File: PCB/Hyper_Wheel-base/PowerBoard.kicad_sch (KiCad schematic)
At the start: 19 parts, among them J2 LIPO, U1 CSD85301Q2, U10 TPS22916CNYFPR, U4 TPS22916CNYFPR, U5 TPS78233DDCR, U6 BQ29700DSER, U7 BQ24074RGTR, U9 CSD85301Q2

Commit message: Base Push
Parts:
- added Rdiv1: 150k, Resistor_SMD:R_0603_1608Metric, symbol Device:R
- added Rdiv2: 300k, Resistor_SMD:R_0603_1608Metric, symbol Device:R
- added U12: TPS22916CNYFPR, Hyper_Wheel:TPS22916-YFP0004ABAB, symbol TPS22916CNYFPR:TPS22916CNYFPR
- CP4: renamed from C4; footprint Capacitor_SMD:C_0201_0603Metric_Pad0.64x0.40mm_HandSolder -> (none)
- J2: footprint (none) -> Connector_JST:JST_EH_B2B-EH-A_1x02_P2.50mm_Vertical
- U1, U9: footprint DQK0006B -> Hyper_Wheel:CDS85301-DQK0006B
- U10, U4: footprint YFP0004ABAB -> Hyper_Wheel:TPS22916-YFP0004ABAB
- U6: footprint DSE0006A -> Hyper_Wheel:BQ29700-DSE0006A
- U7: footprint BQ24074RGTR:QFN50P300X300X100-17N -> Hyper_Wheel:BQ24074-QFN50P300X300X100-17N
- renumbered C1 to CP1, C2 to CP2, C3 to CP3, D1 to DP1, R1 to RP1, R2 to RP2, R3 to RP3, R4 to RP4, R5 to RP5, R6 to RP6
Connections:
- net 3.3V_Regulated: now also U12.A2 (VIN); no longer CP4.1, U5.5 (OUT)
- net GND: now also Rdiv1.1, Rdiv2.2, U12.B1 (GND)
- net ChargerOut renamed ChargerOUT
- net LoadSwitch1EN renamed Load1_Ctrl
- net LoadSwitch1_Vout renamed Load1_Vout
- net LoadSwitch2EN renamed Load2_Ctrl
- net LoadSwitch2_Vout renamed Load2_Vout
- net USB+ renamed Charger+
- new net: CP4.1, U5.5 (OUT)
- new net Cell-Mon: Rdiv1.2, Rdiv2.1
- new net Load3_Ctrl: U12.B2 (ON)
- new net Load3_Vout: U12.A1 (VOUT)
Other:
- moved on the sheet: CP2, CP3, DP1, RP3, RP4, RP5, RP6, U7

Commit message: Main board nearing RevA completion
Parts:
- removed CP4: 1u, symbol Device:C
- removed U12: TPS22916CNYFPR, Hyper_Wheel:TPS22916-YFP0004ABAB, symbol TPS22916CNYFPR:TPS22916CNYFPR
- removed U5: TPS78233DDCR, DDC5_TEX, symbol TPS78233DDCR:TPS78233DDCR
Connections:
- net GND: no longer CP3.1, J2.1 (Pin_1), RP2.2, Rdiv1.1, U7.2 (BAT_2)
- net at U1.6 (D1), U9.6 (D1): now also U1.7 (D1), U9.7 (D1)
- new net Cell+: CP3.1, J2.1 (Pin_1), RP2.2, Rdiv1.1, U7.2 (BAT_2)

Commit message: Added test pads,
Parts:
- added P17, P18, P19, P20: TestPad, TestPoint:TestPoint_Pad_D2.0mm, symbol Connector:Conn_01x01_Pin
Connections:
- net Cell+: now also P17.1 (Pin_1)
- net Cell-: now also P18.1 (Pin_1)
- net ChargerOUT: now also P19.1 (Pin_1)
- net Prot-: now also P20.1 (Pin_1)

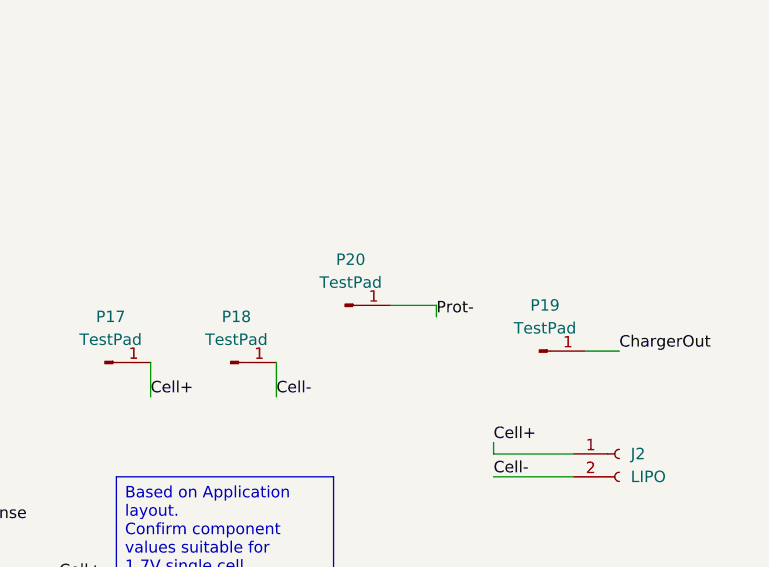
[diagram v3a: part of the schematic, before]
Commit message: XIAO based test board complete
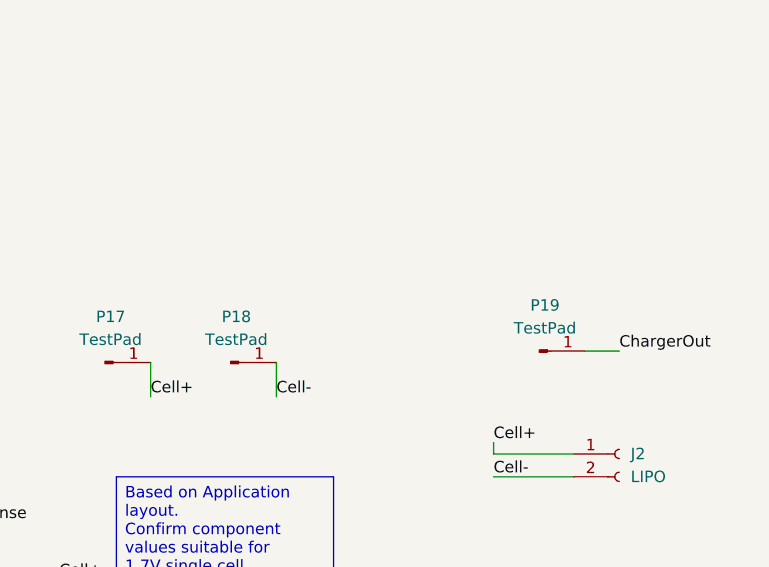
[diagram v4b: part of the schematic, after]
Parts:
- removed P20: TestPad, TestPoint:TestPoint_Pad_D2.0mm, symbol Connector:Conn_01x01_Pin
- CP1, CP2, CP3, DP1, RP1, RP2, RP3, RP4, RP5, RP6, Rdiv1, Rdiv2: KiLib_Generator (none) -> SMD_2terminal_chip_molded
- J2: KiLib_Generator (none) -> connector/JST
- P17, P18, P19: footprint TestPoint:TestPoint_Pad_D2.0mm -> TestPoint:TestPoint_Pad_D1.0mm; now left out of the parts list
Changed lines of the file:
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@@
 	(wire
 		(pts
-			(xy 245.11 71.12) (xy 245.11 72.39)
-		)
-		(stroke
-			(width 0)
-			(type default)
-		)
-	)
-	(wire
-		(pts
 			(xy 101.6 72.39) (xy 109.22 72.39)
 		)
@@
 	(wire
 		(pts
-			(xy 240.03 71.12) (xy 245.11 71.12)
-		)
-		(stroke
-			(width 0)
-			(type default)
-		)
-	)
-	(wire
-		(pts
 			(xy 193.04 137.16) (xy 193.04 162.56)
 		)
@@
 	)
 	(label "Prot-"
-		(at 245.11 72.39 0)
-		(effects
-			(font
-				(size 1.27 1.27)
-			)
-			(justify left bottom)
-		)
-	)
-	(label "Prot-"
 		(at 270.51 110.49 0)
 		(effects
@@
 			)
 		)
+		(property "KiLib_Generator" "SMD_2terminal_chip_molded"
+			(at 123.19 148.59 0)
+			(hide yes)
+			(show_name no)
+			(do_not_autoplace no)
+			(effects
+				(font
+					(size 1.27 1.27)
+				)
+			)
+		)
 		(pin "2"
 		)
@@
 			)
 		)
+		(property "KiLib_Generator" "SMD_2terminal_chip_molded"
+			(at 104.14 182.88 0)
+			(hide yes)
+			(show_name no)
+			(do_not_autoplace no)
+			(effects
+				(font
+					(size 1.27 1.27)
+				)
+			)
+		)
 		(pin "1"
 		)
@@
 		(body_style 1)
 		(exclude_from_sim no)
-		(in_bom yes)
+		(in_bom no)
 		(on_board yes)
 		(in_pos_files yes)
@@
 			)
 		)
-		(property "Footprint" "TestPoint:TestPoint_Pad_D2.0mm"
+		(property "Footprint" "TestPoint:TestPoint_Pad_D1.0mm"
 			(at 222.25 77.47 0)
 			(hide yes)
@@
 			)
 		)
-		(property "Description" "Generic connector, single row, 01x01, script generated"
+		(property "Description" ""
 			(at 222.25 77.47 0)
 			(hide yes)
@@
 	(symbol
 		(lib_id "Connector:Conn_01x01_Pin")
-		(at 234.95 71.12 0)
-		(unit 1)
-		(body_style 1)
-		(exclude_from_sim no)
-		(in_bom yes)
-		(on_board yes)
-		(in_pos_files yes)
-		(dnp no)
-		(fields_autoplaced yes)
-		(property "Reference" "P20"
-			(at 235.585 66.04 0)
-			(show_name no)
-			(do_not_autoplace no)
-			(effects
-				(font
-					(size 1.27 1.27)
-				)
-			)
-		)
-		(property "Value" "TestPad"
-			(at 235.585 68.58 0)
-			(show_name no)
-			(do_not_autoplace no)
-			(effects
-				(font
-					(size 1.27 1.27)
-				)
-			)
-		)
-		(property "Footprint" "TestPoint:TestPoint_Pad_D2.0mm"
-			(at 234.95 71.12 0)
-			(hide yes)
-			(show_name no)
-			(do_not_autoplace no)
-			(effects
-				(font
-					(size 1.27 1.27)
-				)
-			)
-		)
-		(property "Datasheet" ""
-			(at 234.95 71.12 0)
-			(hide yes)
-			(show_name no)
-			(do_not_autoplace no)
-			(effects
-				(font
-					(size 1.27 1.27)
-				)
-			)
-		)
-		(property "Description" "Generic connector, single row, 01x01, script generated"
-			(at 234.95 71.12 0)
-			(hide yes)
-			(show_name no)
-			(do_not_autoplace no)
-			(effects
-				(font
-					(size 1.27 1.27)
-				)
-			)
-		)
-		(pin "1"
-		)
-		(instances
-			(project "Hyper_Wheel-base"
-				(path "/3f05eeb1-03f9-49d1-8a58-0bc3d5427d25/eea2fe20-ac09-4eb8-b37b-43abdbf8377a"
-					(reference "P20")
-					(unit 1)
-				)
-			)
-		)
-	)
-	(symbol
-		(lib_id "Connector:Conn_01x01_Pin")
 		(at 256.54 76.2 0)
 		(unit 1)
 		(body_style 1)
 		(exclude_from_sim no)
-		(in_bom yes)
+		(in_bom no)
 		(on_board yes)
 		(in_pos_files yes)
@@
 			)
 		)
-		(property "Footprint" "TestPoint:TestPoint_Pad_D2.0mm"
+		(property "Footprint" "TestPoint:TestPoint_Pad_D1.0mm"
 			(at 256.54 76.2 0)
 			(hide yes)
@@
 			)
 		)
-		(property "Description" "Generic connector, single row, 01x01, script generated"
+		(property "Description" ""
 			(at 256.54 76.2 0)
 			(hide yes)
@@
 			)
 		)
+		(property "KiLib_Generator" "connector/JST"
+			(at 265.43 87.63 0)
+			(hide yes)
+			(show_name no)
+			(do_not_autoplace no)
+			(effects
+				(font
+					(size 1.27 1.27)
+				)
+			)
+		)
 		(pin "1"
 		)
@@
 			)
 		)
+		(property "KiLib_Generator" "SMD_2terminal_chip_molded"
+			(at 40.64 163.83 0)
+			(hide yes)
+			(show_name no)
+			(do_not_autoplace no)
+			(effects
+				(font
+					(size 1.27 1.27)
+				)
+			)
+		)
 		(pin "1"
 		)
@@
 			)
 		)
+		(property "KiLib_Generator" "SMD_2terminal_chip_molded"
+			(at 59.69 173.99 0)
+			(hide yes)
+			(show_name no)
+			(do_not_autoplace no)
+			(effects
+				(font
+					(size 1.27 1.27)
+				)
+			)
+		)
 		(pin "2"
 		)
@@
 			)
 		)
+		(property "KiLib_Generator" "SMD_2terminal_chip_molded"
+			(at 52.07 168.91 0)
+			(hide yes)
+			(show_name no)
+			(do_not_autoplace no)
+			(effects
+				(font
+					(size 1.27 1.27)
+				)
+			)
+		)
 		(pin "2"
 		)
@@
 			)
 		)
+		(property "KiLib_Generator" "SMD_2terminal_chip_molded"
+			(at 193.04 133.35 0)
+			(hide yes)
+			(show_name no)
+			(do_not_autoplace no)
+			(effects
+				(font
+					(size 1.27 1.27)
+				)
+			)
+		)
 		(pin "1"
 		)
@@
 			)
 		)
+		(property "KiLib_Generator" "SMD_2terminal_chip_molded"
+			(at 240.03 110.49 0)
+			(hide yes)
+			(show_name no)
+			(do_not_autoplace no)
+			(effects
+				(font
+					(size 1.27 1.27)
+				)
+			)
+		)
 		(pin "2"
 		)
@@
 			)
 		)
+		(property "KiLib_Generator" "SMD_2terminal_chip_molded"
+			(at 158.75 50.8 0)
+			(hide yes)
+			(show_name no)
+			(do_not_autoplace no)
+			(effects
+				(font
+					(size 1.27 1.27)
+				)
+			)
+		)
 		(pin "1"
 		)
@@
 			)
 		)
+		(property "KiLib_Generator" "SMD_2terminal_chip_molded"
+			(at 106.68 171.45 0)
+			(hide yes)
+			(show_name no)
+			(do_not_autoplace no)
+			(effects
+				(font
+					(size 1.27 1.27)
+				)
+			)
+		)
 		(pin "2"
 		)
@@
 			)
 		)
+		(property "KiLib_Generator" "SMD_2terminal_chip_molded"
+			(at 193.04 110.49 0)
+			(hide yes)
+			(show_name no)
+			(do_not_autoplace no)
+			(effects
+				(font
+					(size 1.27 1.27)
+				)
+			)
+		)
 		(pin "2"
 		)
@@
 			)
 		)
+		(property "KiLib_Generator" "SMD_2terminal_chip_molded"
+			(at 158.75 66.04 0)
+			(hide yes)
+			(show_name no)
+			(do_not_autoplace no)
+			(effects
+				(font
+					(size 1.27 1.27)
+				)
+			)
+		)
 		(pin "1"
 		)
@@
 		(body_style 1)
 		(exclude_from_sim no)
-		(in_bom yes)
+		(in_bom no)
 		(on_board yes)
 		(in_pos_files yes)
@@
 			)
 		)
-		(property "Footprint" "TestPoint:TestPoint_Pad_D2.0mm"
+		(property "Footprint" "TestPoint:TestPoint_Pad_D1.0mm"
 			(at 208.28 77.47 0)
 			(hide yes)
@@
 			)
 		)
-		(property "Description" "Generic connector, single row, 01x01, script generated"
+		(property "Description" ""
 			(at 208.28 77.47 0)
 			(hide yes)
@@
 			(at 111.76 148.59 0)
 			(hide yes)
+			(show_name no)
+			(do_not_autoplace no)
+			(effects
+				(font
+					(size 1.27 1.27)
+				)
+			)
+		)
+		(property "KiLib_Generator" "SMD_2terminal_chip_molded"
+			(at 111.76 148.59 0)
+			(hide yes)

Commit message: Final cleanup
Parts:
- renumbered P19 to Cell+
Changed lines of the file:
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@@
 		(dnp no)
 		(fields_autoplaced yes)
-		(property "Reference" "P19"
+		(property "Reference" "Cell+"
 			(at 257.175 71.12 0)
 			(show_name no)
@@
 			(project "Hyper_Wheel-base"
 				(path "/3f05eeb1-03f9-49d1-8a58-0bc3d5427d25/eea2fe20-ac09-4eb8-b37b-43abdbf8377a"
-					(reference "P19")
+					(reference "Cell+")
 					(unit 1)
 				)

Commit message: Switched Load switch update
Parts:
- added C23, C24: 1.0u, Capacitor_SMD:C_0603_1608Metric, symbol Device:C
- added C25, C26: 100n, Capacitor_SMD:C_0402_1005Metric, symbol Device:C
- U10, U4: footprint Hyper_Wheel:TPS22916-YFP0004ABAB -> Hyper_Wheel:DBV0006A_L; symbol TPS22916CNYFPR:TPS22916CNYFPR -> Hyper_Wheel:TPS22860DBVR
- renumbered Cell+ to Cell+1
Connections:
- net 3.3V_Regulated: now also U10.4 (VIN), U10.5 (VBIAS), U4.4 (VIN), U4.5 (VBIAS), C23.2, C24.2; no longer U10.A2 (VIN), U4.A2 (VIN)
- net GND: now also U10.2 (GND), U4.2 (GND), C23.1, C24.1, C25.1, C26.1; no longer U10.B1 (GND), U4.B1 (GND)
- net Load1_Ctrl: now also U10.6 (ON); no longer U10.B2 (ON)
- net Load1_Vout: now also U10.1 (VOUT), C25.2; no longer U10.A1 (VOUT)
- net Load2_Ctrl: now also U4.6 (ON); no longer U4.B2 (ON)
- net Load2_Vout: now also U4.1 (VOUT), C26.2; no longer U4.A1 (VOUT)
